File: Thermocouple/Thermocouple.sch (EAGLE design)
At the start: 20 parts, among them Q2 BSS138

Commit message: Latest version of schematics and boards
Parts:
- removed C5: 10uF, SparkFun-Capacitors:CAP0805
- removed LED: blue, led:LEDCHIPLED_1206
- removed Q2: BSS138, SparkFun-DiscreteSemi:MOSFET-NCHANNELBSS138
- added C10, C4: 1uF, SparkFun-Capacitors:CAP0805
- added C12, C6, C8, C9: .1uF, SparkFun-Capacitors:CAP0805
- added C7: .47uF, SparkFun-Capacitors:CAP0805
- added JP2: M023.5MM, SparkFun-Connectors:M023.5MM
- added L1: 1mH, SparkFun-Passives:INDUCTOR1007
- added LED1: (no value), adafruit:LEDCHIP-LED0805
- added R4: 24k, SparkFun-Resistors:RESISTOR0805-RES
- added TP1, TP2, TP3, TP4, TP5, TP6, TP7, TP8, TP9: TEST-POINT3, SparkFun-Passives:TEST-POINT3
- C1: value .1uF -> .47uF
- C2: value 10uF -> .1uF
- JP1: value (none) -> M023.5MM; device SparkFun-Connectors:M04SCREW -> SparkFun-Connectors:M023.5MM
- R1: value 1k -> 680; device SparkFun-Resistors:RESISTOR0805-RES -> SparkFun-Passives:RESISTOR0805-RES
- R2: value 2k -> 1
- R3: value 680 -> 24k; device SparkFun-Passives:RESISTOR0805-RES -> SparkFun-Resistors:RESISTOR0805-RES
- R5, R8: value 1k -> 1M
- R6: value 2k -> 24k
- R7: value 1k -> 24k
- R9: value 2k -> 22; device SparkFun-Resistors:RESISTOR0805-RES -> SparkFun-Passives:RESISTOR0805-RES
- U$1: value MAX31855 -> AD8495; device IntegerLabs:MAX31855 -> IntegerLabs:AD8495
- U$2: value MIC5205-3.3 -> FOOTPRINTFOOTPRINT-2; device SparkFun-PowerIC:V_REG_MIC52053.3V -> IntegerLabs:FOOTPRINTFOOTPRINT-2
- U$3: value TINY841 -> ATTINY48/88-TQFP; device IntegerLabs:TINY841 -> IntegerLabs:ATTINY48/88-TQFP
- U$4: value FOOTPRINT -> AD8495; device IntegerLabs:FOOTPRINT -> IntegerLabs:AD8495
- U$5: value MAX31855 -> zener; device IntegerLabs:MAX31855 -> SparkFun-DiscreteSemi:DIODE-ZENER-BZT52
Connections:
- removed net +3.3V: C3.1, C5.1, U$1.VCC, U$2.OUT, U$5.VCC
- removed net +5V: C1.1, C2.1, R1.2, U$2.EN, U$2.IN, U$3.VCC, U$4.+5V
- removed net CS1: R2.2, U$3.PB0
- removed net CS1-3.3: R2.1, R5.2, U$1.CS
- removed net CS2: R6.2, U$3.PB1
- removed net CS2-3.3: R6.1, R7.2, U$5.CS
- removed net MISO3.3: Q2.G, U$1.MISO, U$5.MISO
- removed net MISO5: Q2.D, R1.1, U$3.PA7
- removed net SCK-3.3: R8.2, R9.1, U$1.SCK, U$5.SCK
- removed net SCL/SCK: U$3.PA4, U$4.SCL
- removed net SDA/MOSI: U$3.PA6, U$4.SDA
- removed net T1+: JP1.4, U$1.T+
- removed net T1-: JP1.3, U$1.T-
- removed net T2+: JP1.2, U$5.T+
- removed net T2-: JP1.1, U$5.T-
- new net AVCC: C7.1, L1.1, TP4.1, TP5.1, U$1.VS+, U$3.AVCC, U$4.VS+, U$5.C
- new net IN1+: JP1.1, R4.1, TP6.1
- new net IN1-: JP1.2, R3.1, R5.2, TP7.1
- new net IN2+: JP2.1, R7.1, TP8.1
- new net IN2-: JP2.2, R6.1, R8.2, TP9.1
- new net MOSI: U$2.MOSI, U$3.PB3
- new net N$2: R2.2, U$2.VCC
- new net N$3: C3.2, C4.1, R3.2, U$1.IN-
- new net N$4: C2.1, C4.2, R4.2, U$1.IN+
- new net N$6: C10.2, C8.1, R7.2, U$4.IN+
- new net N$7: L1.2, R9.1
- new net N$8: LED1.A, R1.1
- new net SCL: U$2.SCL, U$3.PC5
- new net SDA: U$2.SDA, U$3.PC4
- new net TEMP1: C6.1, TP1.1, U$1.OUT, U$1.SENSE, U$3.PA2
- new net TEMP2: C12.1, TP2.1, U$3.PA3, U$4.OUT, U$4.SENSE
- new net VCC: C1.2, R2.1, R9.2, U$2.VPROG, U$3.VCC
- net GND: now also C1.1, C12.2, C3.1, C6.2, C7.2, C8.2, C9.1, LED1.C, TP3.1, U$1.REF, U$1.VS-, U$3.GND@1, U$4.REF, U$4.VS-, U$5.A; no longer C1.2, C3.2, C5.2, LED.C, Q2.S, R7.1, U$1.GND, U$4.GND, U$5.GND
- net LED: now also R1.2, U$3.PB1; no longer R3.2, U$3.PA1
- net MISO: now also U$2.MISO, U$3.PB4; no longer U$3.PA5, U$4.MISO
- net N$5: now also C10.1, C9.2, R6.2, U$4.IN-; no longer LED.A, R3.1
- net RESET: now also U$2.RESET, U$3.PC6; no longer U$3.PB3, U$4.RESET
- net SCK: now also U$2.SCK, U$3.PB5; no longer R9.2, U$3.PB2
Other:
- moved on the sheet: C1, C2, C3, R1, R2, R3, R5, R6, R7, R8, R9

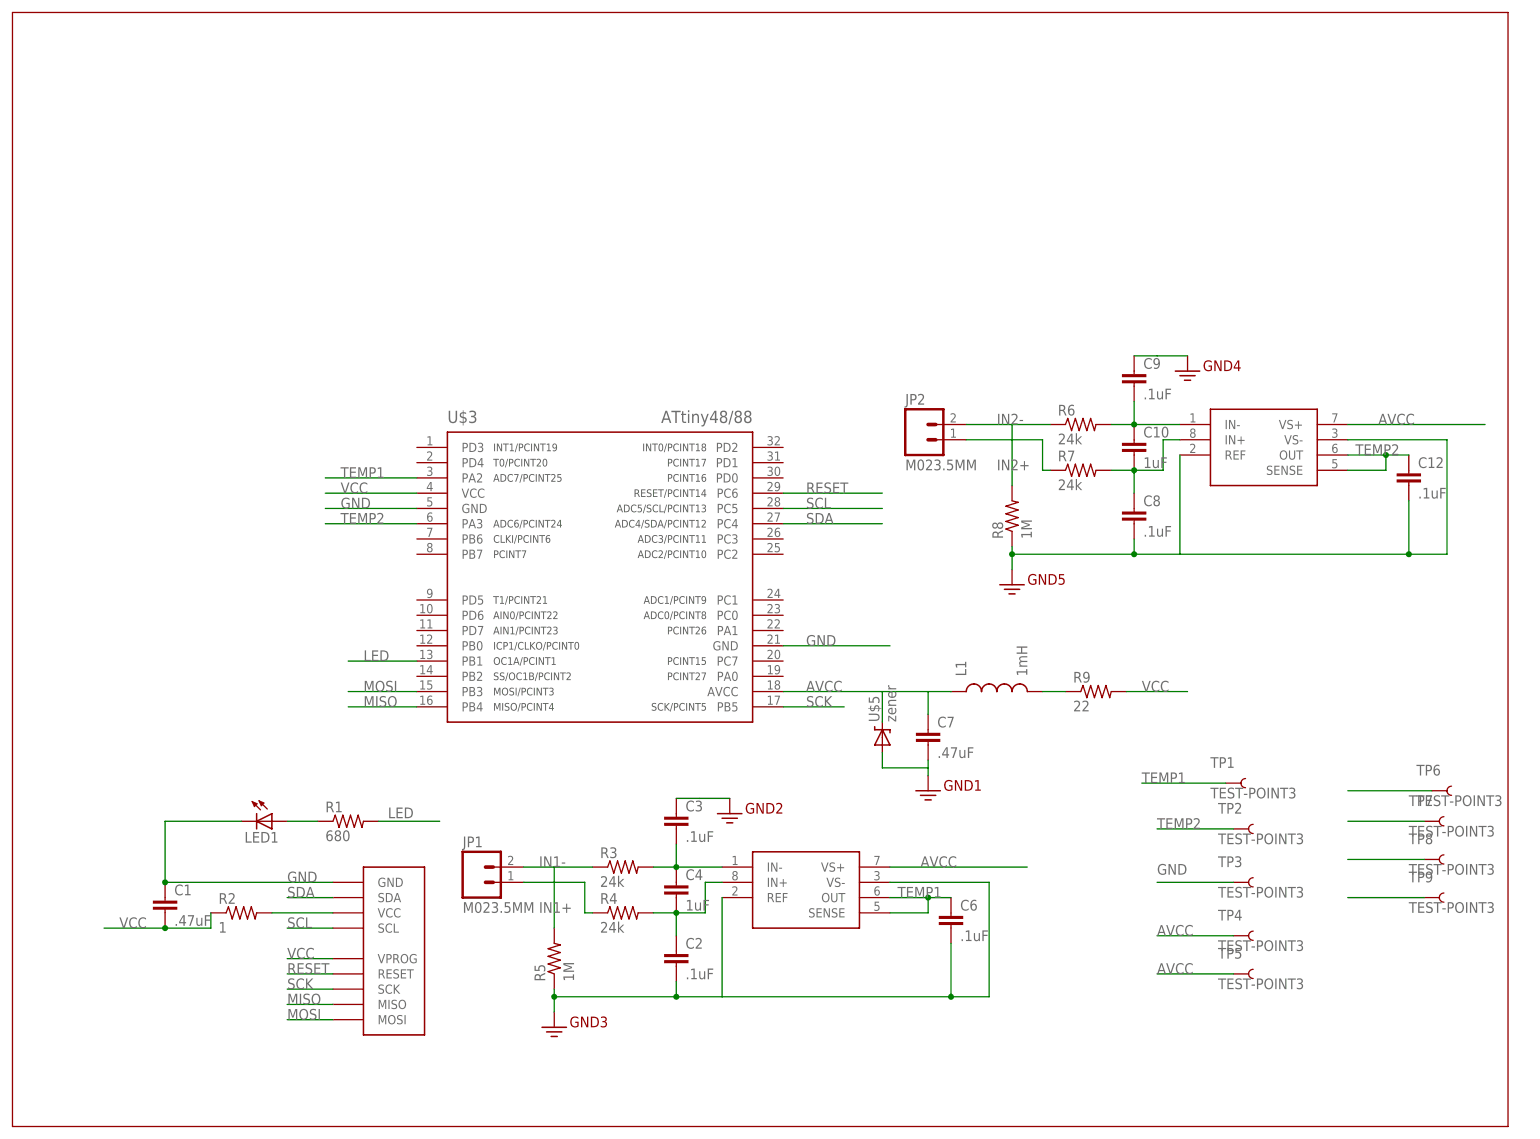
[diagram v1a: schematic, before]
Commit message: OLED: added buttons and rewired for attiny841 Thermocouple: checkpoint of latest version with two amplifiers and attiny48
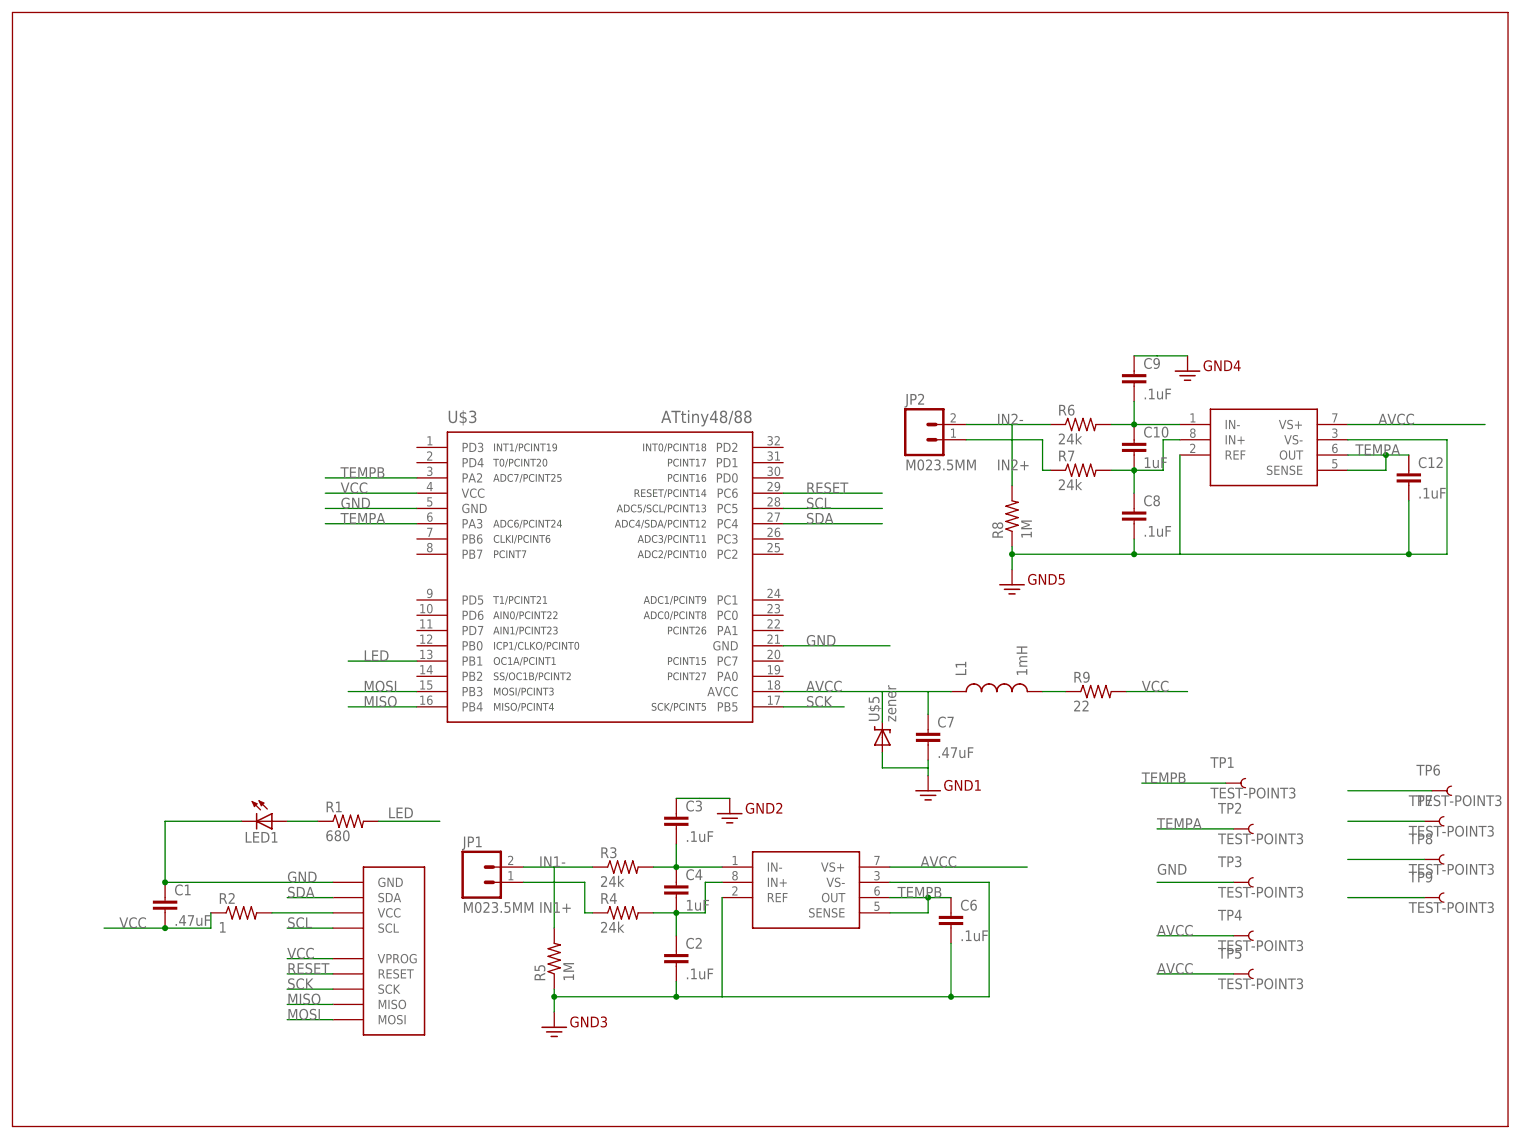
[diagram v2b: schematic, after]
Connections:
- net TEMP1 renamed TEMPB
- net TEMP2 renamed TEMPA
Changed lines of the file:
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@@
 <setting verticaltext="up"/>
 </settings>
-<grid distance="0.05" unitdist="inch" unit="inch" style="lines" multiple="1" display="no" altdistance="0.01" altunitdist="inch" altunit="inch"/>
+<grid distance="0.1" unitdist="inch" unit="inch" style="lines" multiple="1" display="no" altdistance="0.01" altunitdist="inch" altunit="inch"/>
 <layers>
 <layer number="1" name="Top" color="4" fill="1" visible="no" active="no"/>
@@
 </segment>
 </net>
-<net name="TEMP1" class="0">
+<net name="TEMPB" class="0">
 <segment>
 <pinref part="U$1" gate="G$1" pin="OUT"/>
@@
 </segment>
 </net>
-<net name="TEMP2" class="0">
+<net name="TEMPA" class="0">
 <segment>
 <pinref part="U$4" gate="G$1" pin="OUT"/>

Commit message: New thermocouple revision with single input and quick connect terminals
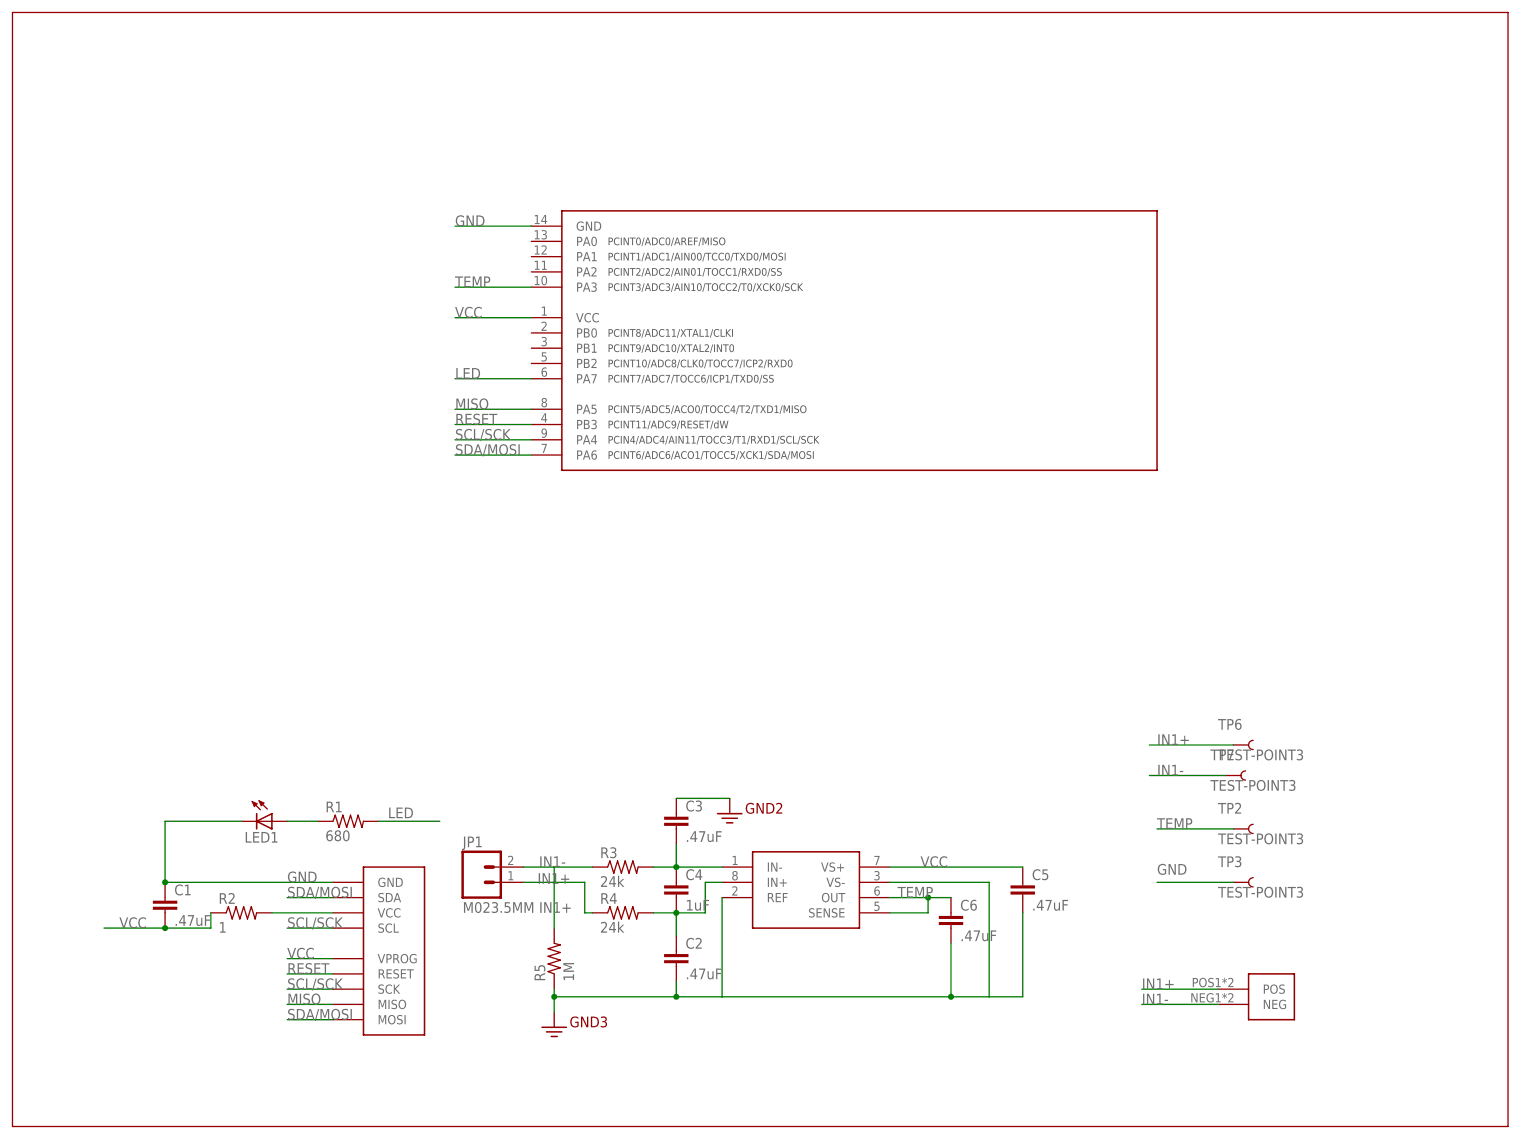
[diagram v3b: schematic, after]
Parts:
- removed C10: 1uF, SparkFun-Capacitors:CAP0805
- removed C12, C8, C9: .1uF, SparkFun-Capacitors:CAP0805
- removed C7: .47uF, SparkFun-Capacitors:CAP0805
- removed JP2: M023.5MM, SparkFun-Connectors:M023.5MM
- removed L1: 1mH, SparkFun-Passives:INDUCTOR1007
- removed R6, R7: 24k, SparkFun-Resistors:RESISTOR0805-RES
- removed R8: 1M, SparkFun-Resistors:RESISTOR0805-RES
- removed R9: 22, SparkFun-Passives:RESISTOR0805-RES
- removed TP1, TP4, TP5, TP8, TP9: TEST-POINT3, SparkFun-Passives:TEST-POINT3
- removed U$5: zener, SparkFun-DiscreteSemi:DIODE-ZENER-BZT52
- added C5: .47uF, SparkFun-Capacitors:CAP0805
- C2, C3, C6: value .1uF -> .47uF
- LED1: device adafruit:LEDCHIP-LED0805 -> adafruit:LEDCHIPLED_0805
- U$3: value ATTINY48/88-TQFP -> TINY841; device IntegerLabs:ATTINY48/88-TQFP -> IntegerLabs:TINY841
- U$4: value AD8495 -> THERMOCOUPLE-JACK; device IntegerLabs:AD8495 -> IntegerLabs:THERMOCOUPLE-JACK
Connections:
- removed net AVCC: C7.1, L1.1, TP4.1, TP5.1, U$1.VS+, U$3.AVCC, U$4.VS+, U$5.C
- removed net IN2+: JP2.1, R7.1, TP8.1
- removed net IN2-: JP2.2, R6.1, R8.2, TP9.1
- removed net MOSI: U$2.MOSI, U$3.PB3
- removed net N$5: C10.1, C9.2, R6.2, U$4.IN-
- removed net N$6: C10.2, C8.1, R7.2, U$4.IN+
- removed net N$7: L1.2, R9.1
- removed net SCK: U$2.SCK, U$3.PB5
- removed net SCL: U$2.SCL, U$3.PC5
- removed net SDA: U$2.SDA, U$3.PC4
- removed net TEMPA: C12.1, TP2.1, U$3.PA3, U$4.OUT, U$4.SENSE
- removed net TEMPB: C6.1, TP1.1, U$1.OUT, U$1.SENSE, U$3.PA2
- new net SCL/SCK: U$2.SCK, U$2.SCL, U$3.PA4
- new net SDA/MOSI: U$2.MOSI, U$2.SDA, U$3.PA6
- new net TEMP: C6.1, TP2.1, U$1.OUT, U$1.SENSE, U$3.PA3
- net GND: now also C5.2; no longer C12.2, C7.2, C8.2, C9.1, R8.1, U$3.GND@1, U$4.REF, U$4.VS-, U$5.A
- net IN1+: now also U$4.POS
- net IN1-: now also U$4.NEG
- net LED: now also U$3.PA7; no longer U$3.PB1
- net MISO: now also U$3.PA5; no longer U$3.PB4
- net RESET: now also U$3.PB3; no longer U$3.PC6
- net VCC: now also C5.1, U$1.VS+; no longer R9.2
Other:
- moved on the sheet: TP6, TP7

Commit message: New versions of IntegerLabs library, RotaryEncoder, and Thermocouple
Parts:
- LED1: device adafruit:LEDCHIPLED_0805 -> adafruit:LEDCHIP-LED0805
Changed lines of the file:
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@@
 <part name="R1" library="SparkFun-Passives" deviceset="RESISTOR" device="0805-RES" value="680"/>
 <part name="U$2" library="IntegerLabs" deviceset="FOOTPRINT" device="FOOTPRINT-2" value="FOOTPRINTFOOTPRINT-2"/>
-<part name="LED1" library="adafruit" deviceset="LED" device="CHIPLED_0805"/>
+<part name="LED1" library="adafruit" deviceset="LED" device="CHIP-LED0805"/>
 <part name="R2" library="SparkFun-Resistors" deviceset="RESISTOR" device="0805-RES" value="1"/>
 <part name="U$1" library="IntegerLabs" deviceset="AD8495" device=""/>

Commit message: Checkpointing PCB designs
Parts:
- U$2: BOARD (none) -> Thermocouple; VERSION (none) -> v5
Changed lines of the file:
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@@
 <layers>
 <layer number="1" name="Top" color="4" fill="1" visible="no" active="no"/>
+<layer number="2" name="Route2" color="1" fill="3" visible="no" active="no"/>
+<layer number="3" name="Route3" color="4" fill="3" visible="no" active="no"/>
+<layer number="14" name="Route14" color="1" fill="6" visible="no" active="no"/>
+<layer number="15" name="Route15" color="4" fill="6" visible="no" active="no"/>
 <layer number="16" name="Bottom" color="1" fill="1" visible="no" active="no"/>
 <layer number="17" name="Pads" color="2" fill="1" visible="no" active="no"/>
@@
 <part name="C1" library="SparkFun-Capacitors" deviceset="CAP" device="0805" value=".47uF"/>
 <part name="R1" library="SparkFun-Passives" deviceset="RESISTOR" device="0805-RES" value="680"/>
-<part name="U$2" library="IntegerLabs" deviceset="FOOTPRINT" device="FOOTPRINT-2" value="FOOTPRINTFOOTPRINT-2"/>
+<part name="U$2" library="IntegerLabs" deviceset="FOOTPRINT" device="FOOTPRINT-2" value="FOOTPRINTFOOTPRINT-2">
+<attribute name="BOARD" value="Thermocouple"/>
+<attribute name="VERSION" value="v5"/>
+</part>
 <part name="LED1" library="adafruit" deviceset="LED" device="CHIP-LED0805"/>
 <part name="R2" library="SparkFun-Resistors" deviceset="RESISTOR" device="0805-RES" value="1"/>

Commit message: Various updates
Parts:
- removed R2: 1, SparkFun-Resistors:RESISTOR0805-RES
- removed TP2, TP3, TP6, TP7: TEST-POINT3, SparkFun-Passives:TEST-POINT3
- removed U$2: FOOTPRINTFOOTPRINT-2, IntegerLabs:FOOTPRINTFOOTPRINT-2
- removed U$3: TINY841, IntegerLabs:TINY841
- added U1: ATTINY841, Modulo:ATTINY841
- added U2: EXCLUDE, Modulo:DEVICE-PCB
- C1, C2, C3, C5, C6: value .47uF -> 100nF; device SparkFun-Capacitors:CAP0805 -> Modulo:CAPACITOR-100NF
- C4: device SparkFun-Capacitors:CAP0805 -> Modulo:CAPACITOR-1UF
- JP1: PARTNUM (none) -> OSTTE020104
- LED1: value (none) -> blue; device adafruit:LEDCHIP-LED0805 -> Modulo:LED-0805-BLUE
- R1: value 680 -> 681Ω; device SparkFun-Passives:RESISTOR0805-RES -> Modulo:RESISTOR-681Ω
- R3, R4: device SparkFun-Resistors:RESISTOR0805-RES -> Modulo:RESISTOR-0603; PARTNUM (none) -> ERJ-3EKF2402V
- R5: device SparkFun-Resistors:RESISTOR0805-RES -> Modulo:RESISTOR-0603; PARTNUM (none) -> ERJ-3EKF1004V
- U$1: PARTNUM (none) -> AD8495ARMZ-R7
- U$4: PARTNUM (none) -> Keystone 3572, 3549
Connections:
- removed net N$2: R2.2, U$2.VCC
- net GND: now also U1.GND, U2.GND; no longer TP3.1, U$2.GND, U$3.GND
- net IN1+: no longer TP6.1
- net IN1-: no longer TP7.1
- net LED: now also U1.PA7; no longer U$3.PA7
- net MISO: now also U1.PA5, U2.MISO; no longer U$2.MISO, U$3.PA5
- net RESET: now also U1.PB3, U2.RESET; no longer U$2.RESET, U$3.PB3
- net SCL/SCK: now also U1.PA4, U2.SCK, U2.SCL; no longer U$2.SCK, U$2.SCL, U$3.PA4
- net SDA/MOSI: now also U1.PA6, U2.MOSI, U2.SDA; no longer U$2.MOSI, U$2.SDA, U$3.PA6
- net TEMP: now also U1.PA3; no longer TP2.1, U$3.PA3
- net VCC: now also U1.VCC, U2.VCC, U2.VPROG; no longer R2.1, U$2.VPROG, U$3.VCC
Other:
- moved on the sheet: LED1, R1, R4
